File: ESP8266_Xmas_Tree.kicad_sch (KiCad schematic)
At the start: 41 parts, among them U1 WeMos_D1_mini

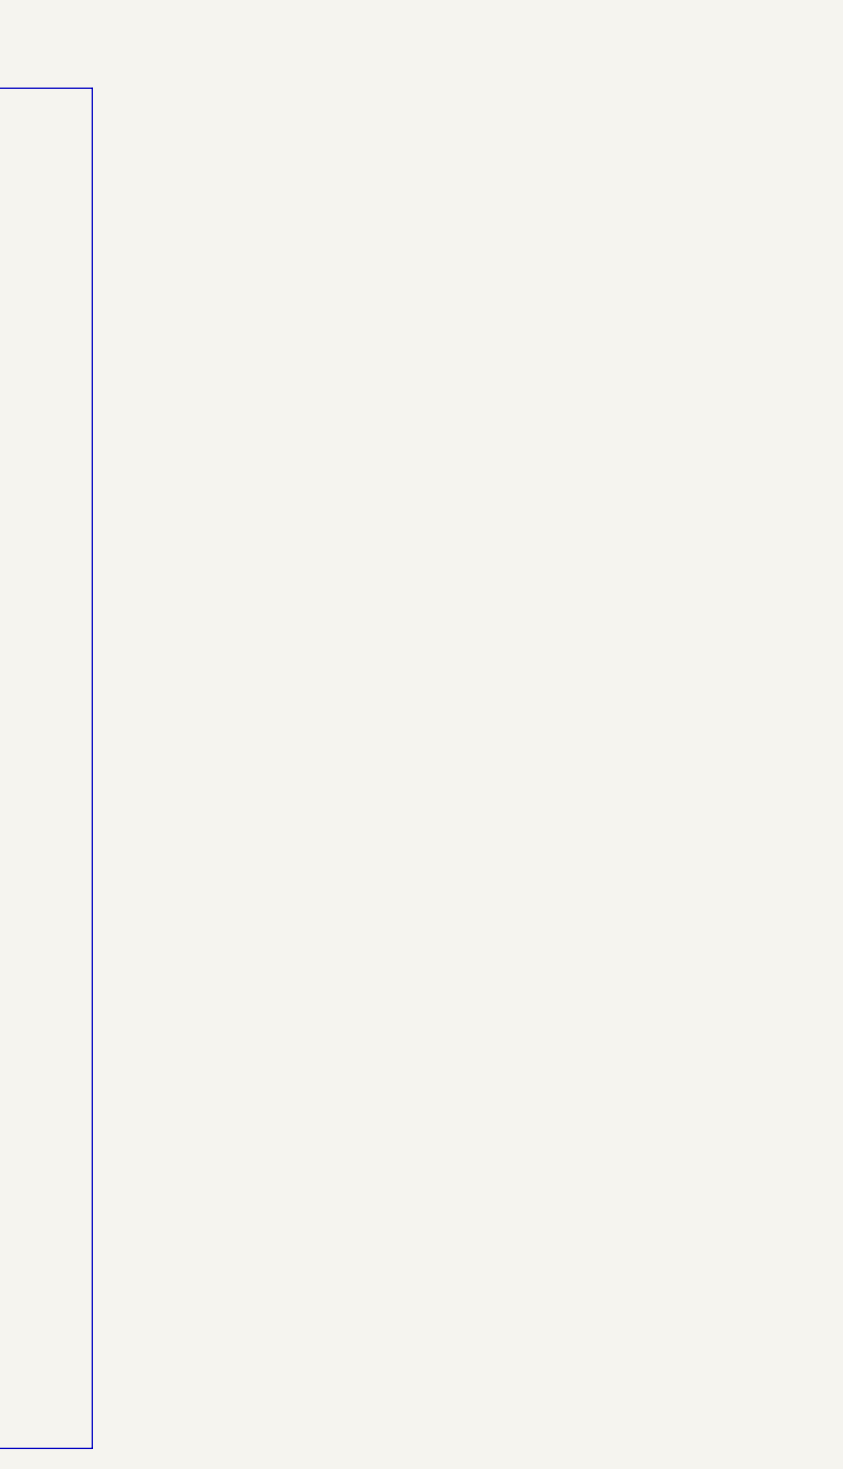
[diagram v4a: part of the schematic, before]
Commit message: adding BMP280 Breakoutboard Lib and footprint to PCB
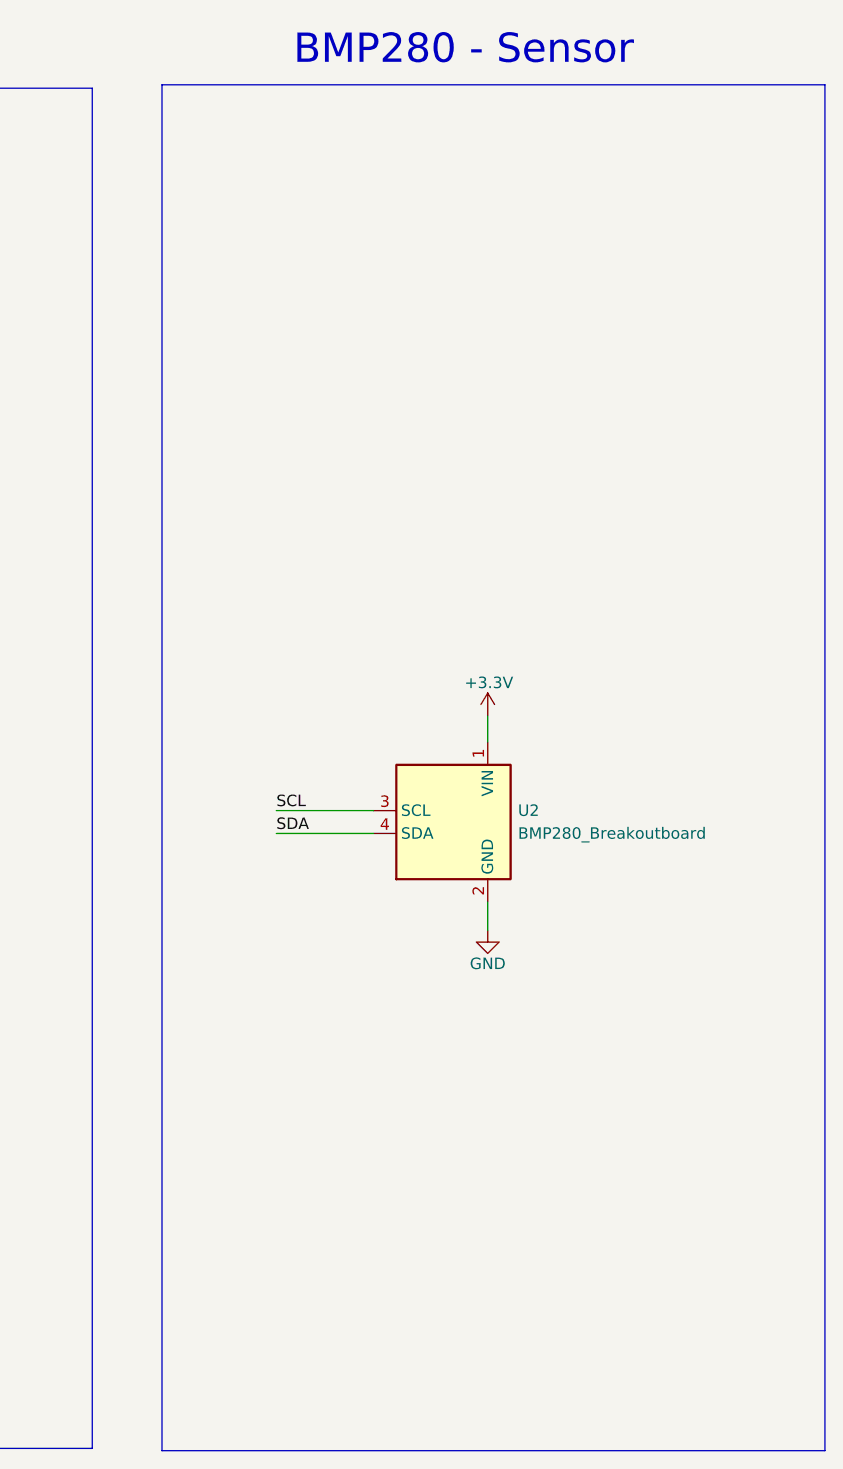
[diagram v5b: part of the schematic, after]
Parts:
- added U2: BMP280_Breakoutboard, BMP280_Breakoutboard:BMP280_Breakoutboard, symbol BMP280_Breakoutboard:BMP280_Breakoutboard
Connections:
- net +3.3V: now also U2.1 (VIN)
- net GND: now also U2.2 (GND)
- net SCL: now also U2.3 (SCL)
- net SDA: now also U2.4 (SDA)
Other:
- note added: "BMP280 - Sensor"
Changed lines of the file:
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@@
+    (stroke (width 0) (type default) (color 0 0 0 0))
+  )
+  (wire (pts (xy 339.09 149.86) (xy 349.885 149.86))
     (stroke (width 0) (type default) (color 0 0 0 0))
   )
@@
     (stroke (width 0) (type default) (color 0 0 0 0))
   )
+  (polyline (pts (xy 400.05 69.215) (xy 400.05 220.98))
+    (stroke (width 0) (type default) (color 0 0 0 0))
+  )
   (wire (pts (xy 278.765 140.335) (xy 299.085 140.335))
     (stroke (width 0) (type default) (color 0 0 0 0))
@@
     (stroke (width 0) (type default) (color 0 0 0 0))
   )
+  (wire (pts (xy 362.585 139.3444) (xy 362.585 142.24))
+    (stroke (width 0) (type default) (color 0 0 0 0))
+  )
   (wire (pts (xy 118.872 181.483) (xy 118.872 182.753))
     (stroke (width 0) (type default) (color 0 0 0 0))
@@
     (stroke (width 0) (type default) (color 0 0 0 0))
   )
+  (polyline (pts (xy 400.05 220.98) (xy 326.39 220.98))
+    (stroke (width 0) (type default) (color 0 0 0 0))
+  )
   (wire (pts (xy 209.042 201.803) (xy 203.962 201.803))
     (stroke (width 0) (type default) (color 0 0 0 0))
@@
     (stroke (width 0) (type default) (color 0 0 0 0))
   )
+  (wire (pts (xy 362.585 160.02) (xy 362.585 163.195))
+    (stroke (width 0) (type default) (color 0 0 0 0))
+  )
   (wire (pts (xy 127.762 175.133) (xy 144.272 175.133))
     (stroke (width 0) (type default) (color 0 0 0 0))
@@
     (stroke (width 0) (type default) (color 0 0 0 0))
   )
+  (wire (pts (xy 339.09 152.4) (xy 349.885 152.4))
+    (stroke (width 0) (type default) (color 0 0 0 0))
+  )
+  (polyline (pts (xy 326.39 69.215) (xy 326.39 220.98))
+    (stroke (width 0) (type default) (color 0 0 0 0))
+  )
   (wire (pts (xy 118.618 133.604) (xy 118.618 134.874))
     (stroke (width 0) (type default) (color 0 0 0 0))
@@
     (stroke (width 0) (type default) (color 0 0 0 0))
   )
+  (polyline (pts (xy 326.39 69.215) (xy 400.05 69.215))
+    (stroke (width 0) (type default) (color 0 0 0 0))
+  )
   (wire (pts (xy 153.162 201.803) (xy 127.762 201.803))
     (stroke (width 0) (type default) (color 0 0 0 0))
@@
   (wire (pts (xy 195.072 175.133) (xy 203.962 175.133))
     (stroke (width 0) (type default) (color 0 0 0 0))
+  )
+  (text "BMP280 - Sensor " (at 340.995 67.31 0)
+    (effects (font (size 3.2512 3.2512)) (justify left bottom))
   )
   (text "WS2812B LEDs" (at 135.255 68.707 0)
@@
   (label "SCL" (at 297.18 150.495 180)
     (effects (font (size 1.27 1.27)) (justify right bottom))
+  )
+  (label "SDA" (at 339.09 152.4 0)
+    (effects (font (size 1.27 1.27)) (justify left bottom))
+  )
+  (label "SCL" (at 339.09 149.86 0)
+    (effects (font (size 1.27 1.27)) (justify left bottom))
   )
   (label "SDA" (at 297.18 153.035 180)
@@
     (pin "1")
   )
+  (symbol (lib_id "power:+3.3V") (at 362.585 139.3444 0) (unit 1)
+    (in_bom yes) (on_board yes)
+    (property "Reference" "#PWR01" (id 0) (at 362.585 143.1544 0)
+      (effects (font (size 1.27 1.27)) hide)
+    )
+    (property "Value" "+3.3V" (id 1) (at 362.712 135.6614 0))
+    (property "Footprint" "" (id 2) (at 362.585 139.3444 0)
+      (effects (font (size 1.27 1.27)) hide)
+    )
+    (property "Datasheet" "" (id 3) (at 362.585 139.3444 0)
+      (effects (font (size 1.27 1.27)) hide)
+    )
+    (pin "1")
+  )
   (symbol (lib_id "LED:WS2812B") (at 127.508 142.494 0) (unit 1)
     (in_bom yes) (on_board yes)
@@
     (pin "4")
   )
+  (symbol (lib_id "power:GND") (at 362.585 163.195 0) (unit 1)
+    (in_bom yes) (on_board yes)
+    (property "Reference" "#PWR010" (id 0) (at 362.585 169.545 0)
+      (effects (font (size 1.27 1.27)) hide)
+    )
+    (property "Value" "GND" (id 1) (at 362.585 166.878 0))
+    (property "Footprint" "" (id 2) (at 362.585 163.195 0)
+      (effects (font (size 1.27 1.27)) hide)
+    )
+    (property "Datasheet" "" (id 3) (at 362.585 163.195 0)
+      (effects (font (size 1.27 1.27)) hide)
+    )
+    (pin "1")
+  )
   (symbol (lib_id "Connector:TestPoint_Small") (at 299.085 137.795 0) (unit 1)
     (in_bom yes) (on_board yes) (fields_autoplaced)
@@
     )
     (pin "1")
+  )
+  (symbol (lib_id "BMP280_Breakoutboard:BMP280_Breakoutboard") (at 358.775 151.13 0) (unit 1)
+    (in_bom yes) (on_board yes) (fields_autoplaced)
+    (property "Reference" "U2" (id 0) (at 365.9378 149.8599 0)
+      (effects (font (size 1.27 1.27)) (justify left))
+    )
+    (property "Value" "BMP280_Breakoutboard" (id 1) (at 365.9378 152.3999 0)
+      (effects (font (size 1.27 1.27)) (justify left))
+    )
+    (property "Footprint" "BMP280_Breakoutboard:BMP280_Breakoutboard" (id 2) (at 358.775 168.91 0)
+      (effects (font (size 1.27 1.27)) hide)
+    )
+    (property "Datasheet" "https://ae-bst.resource.bosch.com/media/_tech/media/datasheets/BST-BMP280-DS001.pdf" (id 3) (at 358.775 151.13 0)
+      (effects (font (size 1.27 1.27)) hide)
+    )
+    (pin "1")
+    (pin "2")
+    (pin "3")
+    (pin "4")
   )
   (symbol (lib_id "power:GND") (at 209.042 204.343 0) (unit 1)
@@
       (reference "#FLG02") (unit 1) (value "PWR_FLAG") (footprint "")
     )
+    (path "/5c851227-6da6-4616-882e-3b8164985648"
+      (reference "#PWR01") (unit 1) (value "+3.3V") (footprint "")
+    )
     (path "/31612f04-02cf-4c5c-86e4-d2e72fc61e1e"
       (reference "#PWR02") (unit 1) (value "GND") (footprint "")
@@
       (reference "#PWR09") (unit 1) (value "+3.3V") (footprint "")
     )
+    (path "/7a555b5f-4cd3-4194-9bda-254b7493f7c4"
+      (reference "#PWR010") (unit 1) (value "GND") (footprint "")
+    )
     (path "/d20cf451-bad9-41b6-97a8-a62692672afb"
       (reference "#PWR011") (unit 1) (value "GND") (footprint "")
@@
       (reference "U1") (unit 1) (value "WeMos_D1_mini") (footprint "Module:WEMOS_D1_mini_light")
     )
-  )
+    (path "/ce0b1a82-0f7e-4590-8254-54634f3098eb"
+      (reference "U2") (unit 1) (value "BMP280_Breakoutboard") (footprint "BMP280_Breakoutboard:BMP280_Breakoutboard")
+    )
+  )
